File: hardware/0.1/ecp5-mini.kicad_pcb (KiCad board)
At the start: 4 copper layers, 52 x 27 mm, 64 parts, among them J1 Micro_SD_Card, J2 JTAG, J3 S7 Mini, J4 S7 Mini, J5 USB_C_Receptacle_USB2.0, Q1 BSS138, SW1 SW_Push, U1 ECP5U_12_CABGA256, U2 TLV73325PDBV, U3 TLV62568DBV, U4 USBLC6-2SC6, U5 TLV62568DBV, U6 W25Q128JVSIQ, U7 S27KL0641

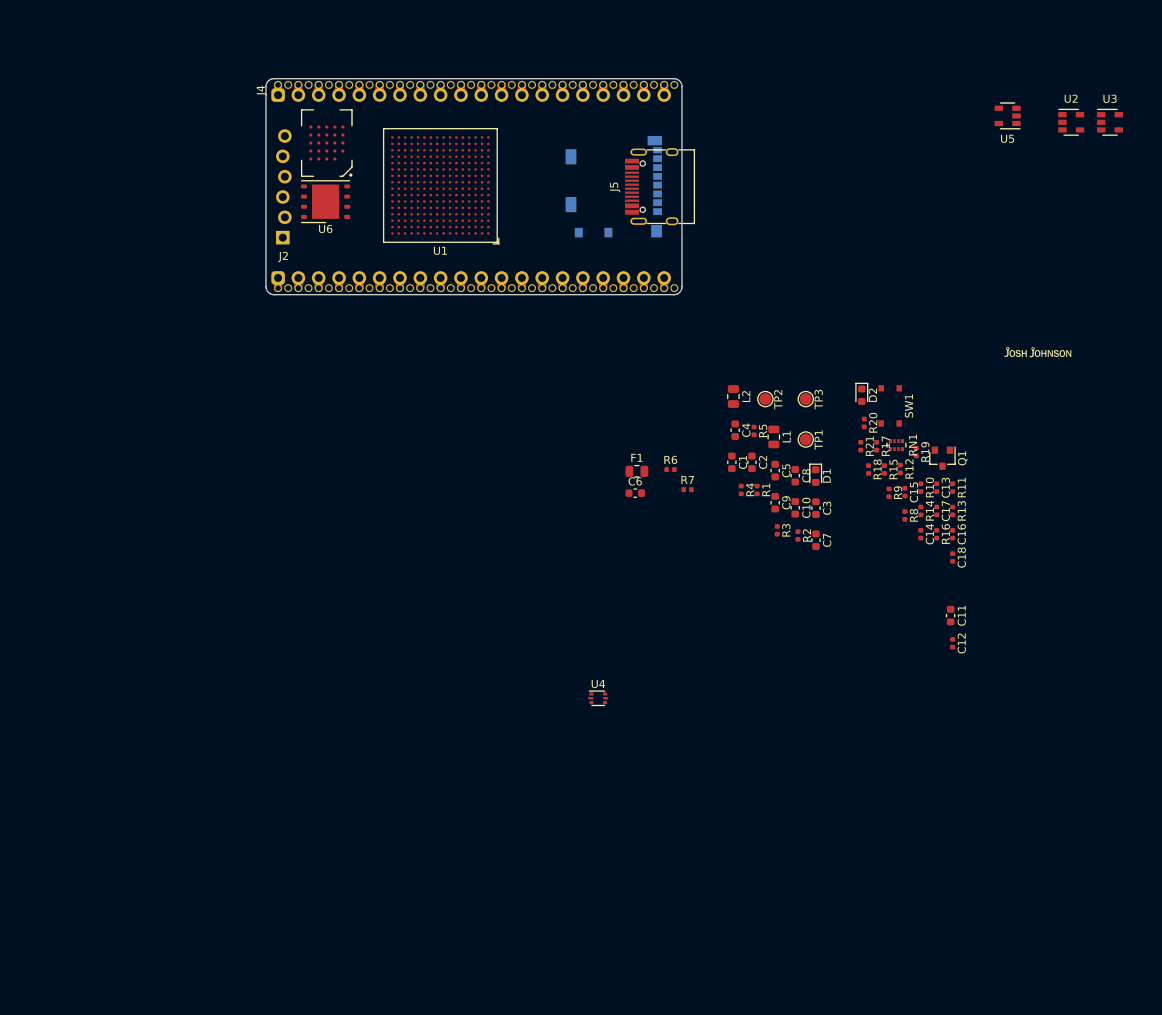
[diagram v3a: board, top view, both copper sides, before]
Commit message: all 3d models added
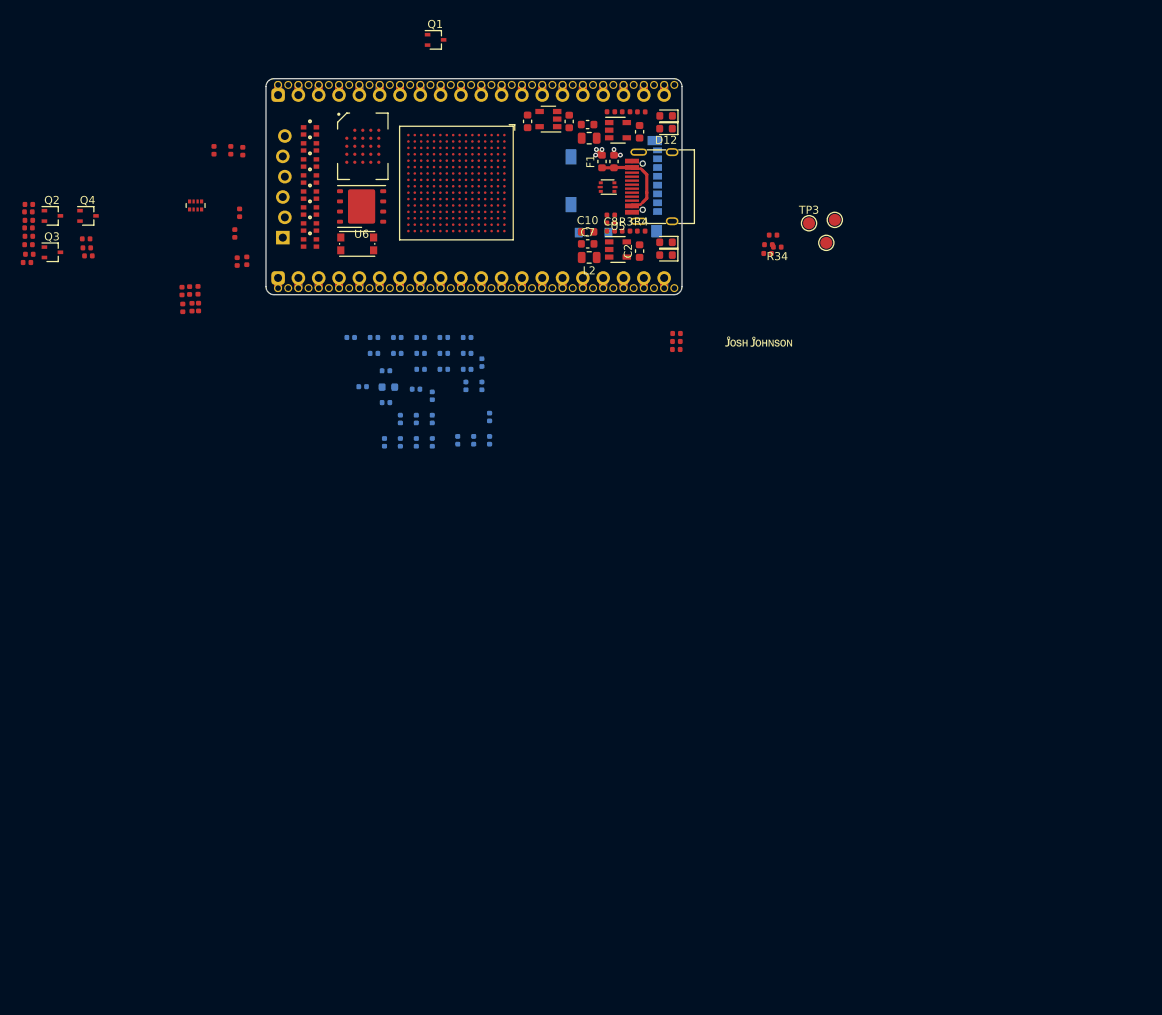
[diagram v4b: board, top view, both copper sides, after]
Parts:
- added C19: 100n, Capacitor_SMD:C_0402_1005Metric, B.Cu at (118.4, 117.8)
- added C20: 100n, Capacitor_SMD:C_0402_1005Metric, B.Cu at (121.3, 113.8)
- added C21: 100n, Capacitor_SMD:C_0402_1005Metric, B.Cu at (118.4, 115.8)
- added C22: 100n, Capacitor_SMD:C_0402_1005Metric, B.Cu at (120.2, 126.7)
- added C23: 470n, Capacitor_SMD:C_0402_1005Metric, B.Cu at (115.5, 115.8)
- added C24: 470n, Capacitor_SMD:C_0402_1005Metric, B.Cu at (124.2, 126.7)
- added C25: 100n, Capacitor_SMD:C_0402_1005Metric, B.Cu at (112.6, 113.8)
- added C26: 100n, Capacitor_SMD:C_0402_1005Metric, B.Cu at (115.5, 117.8)
- added C27: 100n, Capacitor_SMD:C_0402_1005Metric, B.Cu at (121.3, 115.8)
- added C28: 100n, Capacitor_SMD:C_0402_1005Metric, B.Cu at (112.6, 115.8)
- added C29: 470n, Capacitor_SMD:C_0402_1005Metric, B.Cu at (118.4, 113.8)
- added C30: 470n, Capacitor_SMD:C_0402_1005Metric, B.Cu at (121.3, 117.8)
- added C31: 100n, Capacitor_SMD:C_0402_1005Metric, B.Cu at (124.2, 123.7)
- added C32: 100n, Capacitor_SMD:C_0402_1005Metric, B.Cu at (109.7, 113.8)
- added C33: 100n, Capacitor_SMD:C_0402_1005Metric, B.Cu at (106.8, 113.8)
- added C34: 100n, Capacitor_SMD:C_0402_1005Metric, B.Cu at (109.7, 115.8)
- added C35: 470n, Capacitor_SMD:C_0402_1005Metric, B.Cu at (122.2, 126.7)
- added C36: 470n, Capacitor_SMD:C_0402_1005Metric, B.Cu at (115.5, 113.8)
- added C37: 100n, Capacitor_SMD:C_0402_1005Metric, B.Cu at (117.0, 124.0)
- added C38: 100n, Capacitor_SMD:C_0402_1005Metric, B.Cu at (115.0, 124.0)
- added C39: 100n, Capacitor_SMD:C_0402_1005Metric, B.Cu at (115.0, 126.9)
- added C40: 100n, Capacitor_SMD:C_0402_1005Metric, B.Cu at (117.0, 126.9)
- added C41: 100n, Capacitor_SMD:C_0402_1005Metric, B.Cu at (113.0, 124.0)
- added C42: 100n, Capacitor_SMD:C_0402_1005Metric, B.Cu at (111.0, 126.9)
- added C43: 100n, Capacitor_SMD:C_0402_1005Metric, B.Cu at (117.0, 121.1)
- added C44: 100n, Capacitor_SMD:C_0402_1005Metric, B.Cu at (113.0, 126.9)
- added C45: 100n, Capacitor_SMD:C_0402_1005Metric, B.Cu at (123.2, 116.9)
- added C46: 100n, Capacitor_SMD:C_0402_1005Metric, B.Cu at (123.2, 119.8)
- added C47: 100n, Capacitor_SMD:C_0402_1005Metric, B.Cu at (121.2, 119.8)
- added D10: LED_RGBA, josh-led:LED_0606_E6C0606RGBC3UDA, F.Cu at (101.7, 102.0)
- added D11: LED_RGBA, josh-led:LED_0606_E6C0606RGBC3UDA, F.Cu at (101.7, 88.0)
- added D12: PINK, LED_SMD:LED_0603_1608Metric, F.Cu at (146.2, 87.7)
- added D3: PINK, LED_SMD:LED_0603_1608Metric, F.Cu at (146.2, 86.1)
- added D4: LED_RGBA, josh-led:LED_0606_E6C0606RGBC3UDA, F.Cu at (101.7, 92.0)
- added D5: LED_RGBA, josh-led:LED_0606_E6C0606RGBC3UDA, F.Cu at (101.7, 90.0)
- added D6: LED_RGBA, josh-led:LED_0606_E6C0606RGBC3UDA, F.Cu at (101.7, 94.0)
- added D7: LED_RGBA, josh-led:LED_0606_E6C0606RGBC3UDA, F.Cu at (101.7, 100.0)
- added D8: LED_RGBA, josh-led:LED_0606_E6C0606RGBC3UDA, F.Cu at (101.7, 98.0)
- added D9: LED_RGBA, josh-led:LED_0606_E6C0606RGBC3UDA, F.Cu at (101.7, 96.0)
- added Q2: BSS138, Package_TO_SOT_SMD:SOT-323_SC-70, F.Cu at (69.5, 98.6)
- added Q3: BSS138, Package_TO_SOT_SMD:SOT-323_SC-70, F.Cu at (69.5, 103.2)
- added Q4: BSS138, Package_TO_SOT_SMD:SOT-323_SC-70, F.Cu at (74.0, 98.6)
- added R22: 1K5, Resistor_SMD:R_0402_1005Metric, F.Cu at (158.9, 103.3)
- added R23: 220R, Resistor_SMD:R_0402_1005Metric, F.Cu at (66.6, 101.2)
- added R24: 220R, Resistor_SMD:R_0402_1005Metric, F.Cu at (66.6, 97.2)
- added R25: 10K, Resistor_SMD:R_0402_1005Metric, F.Cu at (73.8, 102.6)
- added R26: 220R, Resistor_SMD:R_0402_1005Metric, F.Cu at (66.5, 102.2)
- added R27: 220R, Resistor_SMD:R_0402_1005Metric, F.Cu at (66.3, 104.4)
- added R28: 10K, Resistor_SMD:R_0402_1005Metric, F.Cu at (73.7, 101.5)
- added R29: 220R, Resistor_SMD:R_0402_1005Metric, F.Cu at (66.6, 99.2)
- added R30: 10K, Resistor_SMD:R_0402_1005Metric, F.Cu at (74.0, 103.6)
- added R31: 220R, Resistor_SMD:R_0402_1005Metric, F.Cu at (66.5, 100.1)
- added R32: 220R, Resistor_SMD:R_0402_1005Metric, F.Cu at (66.5, 98.1)
- added R33: 220R, Resistor_SMD:R_0402_1005Metric, F.Cu at (66.6, 103.4)
- added R34: 1K5, Resistor_SMD:R_0402_1005Metric, F.Cu at (160.1, 102.5)
- C10: value 6p8 -> 22u
- C11, C12, C14, C16, C17: moved to B.Cu
- C8: value 22u -> 6p8; footprint Capacitor_SMD:C_0603_1608Metric -> Capacitor_SMD:C_0402_1005Metric
- C9: footprint Capacitor_SMD:C_0603_1608Metric -> Capacitor_SMD:C_0402_1005Metric
- F1: footprint josh-passives-smt:Fuse_0805_2012Metric -> josh-passives-smt:Fuse_0603_1608Metric
- J1: footprint Connector_Card:microSD_HC_Molex_104031-0811 -> josh-mechanical:microSD_HC_Molex_104031-0811
- Q1: footprint Package_TO_SOT_SMD:SOT-23 -> Package_TO_SOT_SMD:SOT-323_SC-70
- R5: value 5K1 -> 1K5
- SW1: footprint josh-buttons-switches:SW_Push_PTS815 -> josh-buttons-switches:SW_Push_KMR2
- U6: footprint Package_SON:WSON-8-1EP_6x5mm_P1.27mm_EP3.4x4.3mm -> josh-soic-sot-etc:WSON-8-1EP_6x5mm_P1.27mm_EP3.4x4.3mm
- moved C18 98.5 mm to (92.3, 100.8)
- moved R13 97.6 mm to (87.8, 110.0)
- moved R16 97.3 mm to (87.0, 110.0)
- moved R14 95.7 mm to (85.8, 110.1)
- moved R19 93.6 mm to (91.8, 90.4)
- moved C15 93.1 mm to (93.3, 90.5)
- moved RN1 92.6 mm to (87.4, 97.3)
- moved C13 91.9 mm to (92.6, 104.3)
- moved R8 91.4 mm to (92.9, 98.2)
- moved R17 89.0 mm to (85.7, 108.0)
- moved R15 88.7 mm to (87.7, 107.9)
- moved R20 88.1 mm to (89.7, 90.4)
- moved R18 87.8 mm to (86.7, 107.9)
- moved R12 85.7 mm to (93.8, 104.2)
- moved Q1 82.1 mm to (117.4, 76.6), turned to 0 degrees
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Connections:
- net Net-(J3-Pad1) renamed /Board IO/PORT_A0
- net Net-(J3-Pad11) renamed /Board IO/PORT_B0
- net Net-(J3-Pad12) renamed /Board IO/PORT_B4
- net Net-(J3-Pad13) renamed /Board IO/PORT_B1
- net Net-(J3-Pad14) renamed /Board IO/PORT_B5
- net Net-(J3-Pad15) renamed /Board IO/PORT_B2
- net Net-(J3-Pad16) renamed /Board IO/PORT_B6
- net Net-(J3-Pad17) renamed /Board IO/PORT_B3
- net Net-(J3-Pad18) renamed /Board IO/PORT_B7
- net Net-(J3-Pad2) renamed /Board IO/PORT_A4
- net Net-(J3-Pad21) renamed /Board IO/PORT_C0
- net Net-(J3-Pad22) renamed /Board IO/PORT_C4
- net Net-(J3-Pad23) renamed /Board IO/PORT_C1
- net Net-(J3-Pad24) renamed /Board IO/PORT_C5
- net Net-(J3-Pad25) renamed /Board IO/PORT_C2
- net Net-(J3-Pad26) renamed /Board IO/PORT_C6
- net Net-(J3-Pad27) renamed /Board IO/PORT_C3
- net Net-(J3-Pad28) renamed /Board IO/PORT_C7
- net Net-(J3-Pad3) renamed /Board IO/PORT_A1
- net Net-(J3-Pad31) renamed /Board IO/PORT_D0
- net Net-(J3-Pad32) renamed /Board IO/PORT_D4
- net Net-(J3-Pad33) renamed /Board IO/PORT_D1
- net Net-(J3-Pad34) renamed /Board IO/PORT_D5
- net Net-(J3-Pad35) renamed /Board IO/PORT_D2
- net Net-(J3-Pad36) renamed /Board IO/PORT_D6
- net Net-(J3-Pad37) renamed /Board IO/PORT_D3
- net Net-(J3-Pad38) renamed /Board IO/PORT_D7
- net Net-(J3-Pad4) renamed /Board IO/PORT_A5
- net Net-(J3-Pad5) renamed /Board IO/PORT_A2
- net Net-(J3-Pad6) renamed /Board IO/PORT_A6
- net Net-(J3-Pad7) renamed /Board IO/PORT_A3
- net Net-(J3-Pad8) renamed /Board IO/PORT_A7
- net Net-(J4-Pad21) renamed /Board IO/PORT_F0
- net Net-(J4-Pad22) renamed /Board IO/PORT_F4
- net Net-(J4-Pad23) renamed /Board IO/PORT_F1
- net Net-(J4-Pad24) renamed /Board IO/PORT_F5
- net Net-(J4-Pad25) renamed /Board IO/PORT_F2
- net Net-(J4-Pad26) renamed /Board IO/PORT_F6
- net Net-(J4-Pad27) renamed /Board IO/PORT_F3
- net Net-(J4-Pad28) renamed /Board IO/PORT_F7
- net Net-(J4-Pad31) renamed /Board IO/PORT_E0
- net Net-(J4-Pad32) renamed /Board IO/PORT_E4
- net Net-(J4-Pad33) renamed /Board IO/PORT_E1
- net Net-(J4-Pad34) renamed /Board IO/PORT_E5
- net Net-(J4-Pad35) renamed /Board IO/PORT_E2
- net Net-(J4-Pad36) renamed /Board IO/PORT_E6
- net Net-(J4-Pad37) renamed /Board IO/PORT_E3
- net Net-(J4-Pad38) renamed /Board IO/PORT_E7
- net Net-(U7-PadA3) renamed /Hyperram / Micro SD/nCS
- net Net-(U7-PadA4) renamed /Hyperram / Micro SD/nRST
- net Net-(U7-PadB1) renamed /Hyperram / Micro SD/nCK
- net Net-(U7-PadB2) renamed /Hyperram / Micro SD/CK
- net Net-(U7-PadC3) renamed /Hyperram / Micro SD/RWDS
- net Net-(U7-PadC4) renamed /Hyperram / Micro SD/DQ2
- net Net-(U7-PadD2) renamed /Hyperram / Micro SD/DQ1
- net Net-(U7-PadD3) renamed /Hyperram / Micro SD/DQ0
- net Net-(U7-PadD4) renamed /Hyperram / Micro SD/DQ3
- net Net-(U7-PadD5) renamed /Hyperram / Micro SD/DQ4
- net Net-(U7-PadE1) renamed /Hyperram / Micro SD/DQ7
- net Net-(U7-PadE2) renamed /Hyperram / Micro SD/DQ6
- net Net-(U7-PadE3) renamed /Hyperram / Micro SD/DQ5
- C10 pad 2: Net-(C10-Pad2) -> GND
- C5 pad 2: Net-(C5-Pad2) -> GND
- C7 pad 2: Net-(C10-Pad2) -> GND
- C8 pad 2: Net-(C10-Pad2) -> Net-(C8-Pad2)
- C9 pad 2: Net-(C5-Pad2) -> Net-(C9-Pad2)
- J3 pad 10: Net-(J3-Pad10) -> GND
- J3 pad 19: Net-(J3-Pad19) -> +3V3
- J3 pad 20: Net-(J3-Pad20) -> GND
- J3 pad 29: Net-(J3-Pad29) -> GND
- J3 pad 30: Net-(J3-Pad30) -> GND
- J3 pad 39: Net-(J3-Pad39) -> +5V
- J3 pad 40: Net-(J3-Pad40) -> GND
- J3 pad 9: Net-(J3-Pad9) -> GND
- J4 pad 1: Net-(J4-Pad1) -> /Board IO/PORT_G0
- J4 pad 10: Net-(J4-Pad10) -> GND
- J4 pad 11: Net-(J4-Pad11) -> /Board IO/PORT_G0
- J4 pad 12: Net-(J4-Pad12) -> /Board IO/PORT_G4
- J4 pad 13: Net-(J4-Pad13) -> /Board IO/PORT_G1
- J4 pad 14: Net-(J4-Pad14) -> /Board IO/PORT_G5
- J4 pad 15: Net-(J4-Pad15) -> /Board IO/PORT_G2
- J4 pad 16: Net-(J4-Pad16) -> /Board IO/PORT_G6
- J4 pad 17: Net-(J4-Pad17) -> /Board IO/PORT_G3
- J4 pad 18: Net-(J4-Pad18) -> /Board IO/PORT_G7
- J4 pad 19: Net-(J4-Pad19) -> +3V3
- J4 pad 2: Net-(J4-Pad2) -> /Board IO/PORT_G4
- J4 pad 20: Net-(J4-Pad20) -> GND
- J4 pad 29: Net-(J4-Pad29) -> GND
- J4 pad 3: Net-(J4-Pad3) -> /Board IO/PORT_G1
- J4 pad 30: Net-(J4-Pad30) -> GND
- J4 pad 39: Net-(J4-Pad39) -> +5V
- J4 pad 4: Net-(J4-Pad4) -> /Board IO/PORT_G5
- J4 pad 40: Net-(J4-Pad40) -> GND
- J4 pad 5: Net-(J4-Pad5) -> /Board IO/PORT_G2
- J4 pad 6: Net-(J4-Pad6) -> /Board IO/PORT_G6
- J4 pad 7: Net-(J4-Pad7) -> /Board IO/PORT_G3
- J4 pad 8: Net-(J4-Pad8) -> /Board IO/PORT_G7
- J4 pad 9: Net-(J4-Pad9) -> GND
- R1 pad 2: Net-(C5-Pad2) -> Net-(C9-Pad2)
- R2 pad 1: Net-(C5-Pad2) -> Net-(C9-Pad2)
- R3 pad 2: Net-(C10-Pad2) -> Net-(C8-Pad2)
- R4 pad 1: Net-(C10-Pad2) -> Net-(C8-Pad2)
- R5 pad 1: +5V -> +3V3
- U1 pad A1: Net-(U1-PadA1) -> GND
- U1 pad A16: Net-(U1-PadA1) -> GND
- U1 pad D15: Net-(U1-PadA1) -> GND
- U1 pad D2: Net-(U1-PadA1) -> GND
- U1 pad F10: Net-(U1-PadF10) -> +3V3
- U1 pad F11: Net-(U1-PadF10) -> +3V3
- U1 pad F6: Net-(U1-PadF6) -> +3V3
- U1 pad F7: Net-(U1-PadF6) -> +3V3
- U1 pad F8: Net-(U1-PadA1) -> GND
- U1 pad F9: Net-(U1-PadA1) -> GND
- U1 pad G10: Net-(U1-PadA1) -> GND
- U1 pad G11: Net-(U1-PadG11) -> +2V5
- U1 pad G6: Net-(U1-PadG6) -> +1V1
- U1 pad G7: Net-(U1-PadG6) -> +1V1
- U1 pad G8: Net-(U1-PadA1) -> GND
- U1 pad G9: Net-(U1-PadG6) -> +1V1
- U1 pad H1: Net-(U1-PadA1) -> GND
- U1 pad H10: Net-(U1-PadA1) -> GND
- U1 pad H11: Net-(U1-PadH11) -> +3V3
- U1 pad H16: Net-(U1-PadA1) -> GND
- U1 pad H6: Net-(U1-PadH6) -> +3V3
- U1 pad H7: Net-(U1-PadH6) -> +3V3
- U1 pad H8: Net-(U1-PadA1) -> GND
- U1 pad H9: Net-(U1-PadA1) -> GND
- U1 pad J10: Net-(U1-PadA1) -> GND
- U1 pad J11: Net-(U1-PadH11) -> +3V3
- U1 pad J6: Net-(U1-PadJ6) -> +3V3
- U1 pad J7: Net-(U1-PadJ6) -> +3V3
- U1 pad J8: Net-(U1-PadA1) -> GND
- U1 pad J9: Net-(U1-PadA1) -> GND
- U1 pad K10: Net-(U1-PadA1) -> GND
- U1 pad K11: Net-(U1-PadK11) -> +3V3
- U1 pad K6: Net-(U1-PadA1) -> GND
- U1 pad K7: Net-(U1-PadA1) -> GND
- U1 pad K8: Net-(U1-PadA1) -> GND
- U1 pad K9: Net-(U1-PadA1) -> GND
- U1 pad L10: Net-(U1-PadG6) -> +1V1
- U1 pad L11: Net-(U1-PadK11) -> +3V3
- U1 pad L7: Net-(U1-PadG11) -> +2V5
- U1 pad L8: Net-(U1-PadG6) -> +1V1
- U1 pad L9: Net-(U1-PadG6) -> +1V1
- U1 pad N15: Net-(U1-PadA1) -> GND
- U1 pad N2: Net-(U1-PadA1) -> GND
- U1 pad R6: Net-(U1-PadR6) -> /FPGA Config/FPGA_OK
- U1 pad T1: Net-(U1-PadA1) -> GND
- U1 pad T12: Net-(U1-PadA1) -> GND
- U1 pad T16: Net-(U1-PadA1) -> GND
- U1 pad T5: Net-(U1-PadA1) -> GND
- U1 pad T6: Net-(U1-PadT6) -> /FPGA Config/LED_USR
- U3 pad 5: Net-(C5-Pad2) -> Net-(C9-Pad2)
- U5 pad 5: Net-(C10-Pad2) -> Net-(C8-Pad2)
- U7 pad B3: Net-(U7-PadB3) -> GND
- U7 pad B4: Net-(U7-PadB4) -> +3V3
- U7 pad C1: Net-(U7-PadC1) -> GND
- U7 pad D1: Net-(U7-PadD1) -> +3V3
- U7 pad E4: Net-(U7-PadE4) -> +3V3
- U7 pad E5: Net-(U7-PadE5) -> GND
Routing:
- net +5V: track 0.00 -> 42.2 mm, vias 0 -> 3
- net Net-(C6-Pad1): track 0.00 -> 13.5 mm
- net GND: track 0.00 -> 1.82 mm, vias 0 -> 2
- added copper zone on In2.Cu, net +3V3
- added copper zone on In1.Cu, net GND

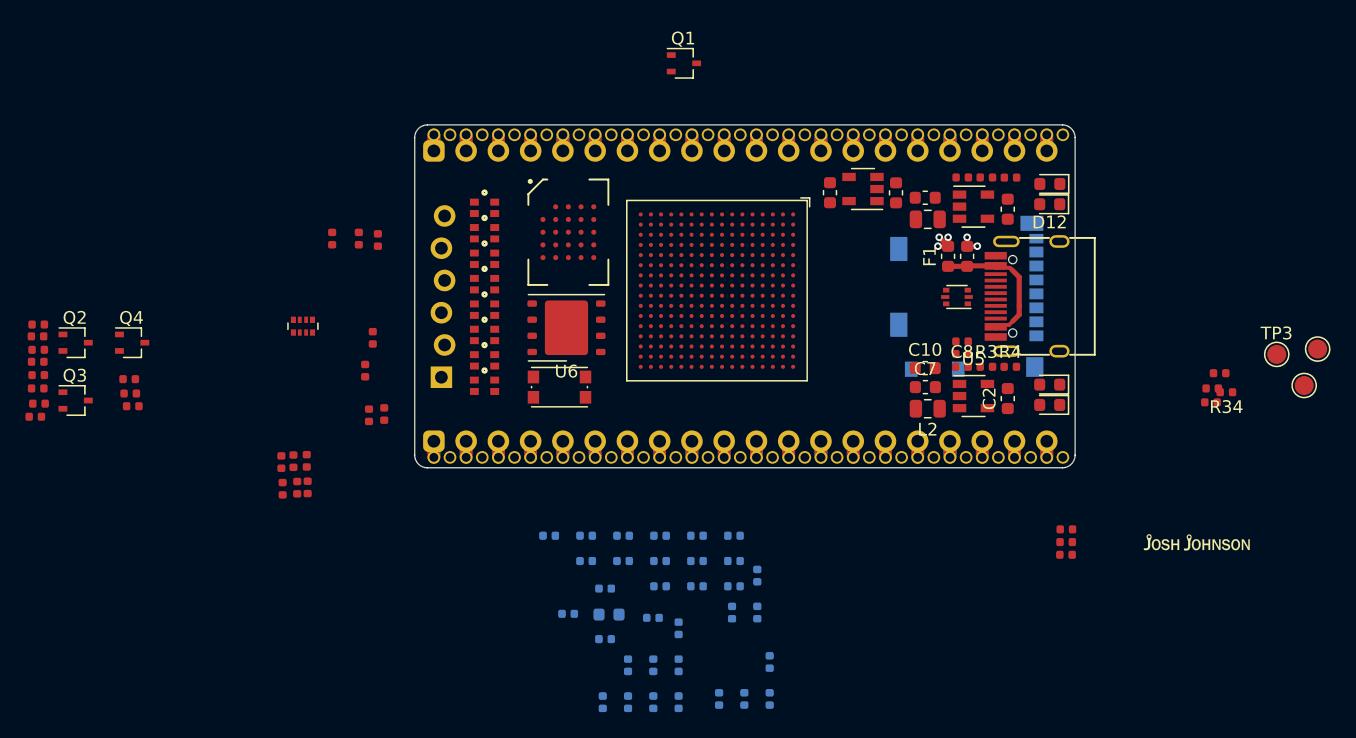
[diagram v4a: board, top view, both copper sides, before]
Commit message: decoupling down + outer pins fanned out
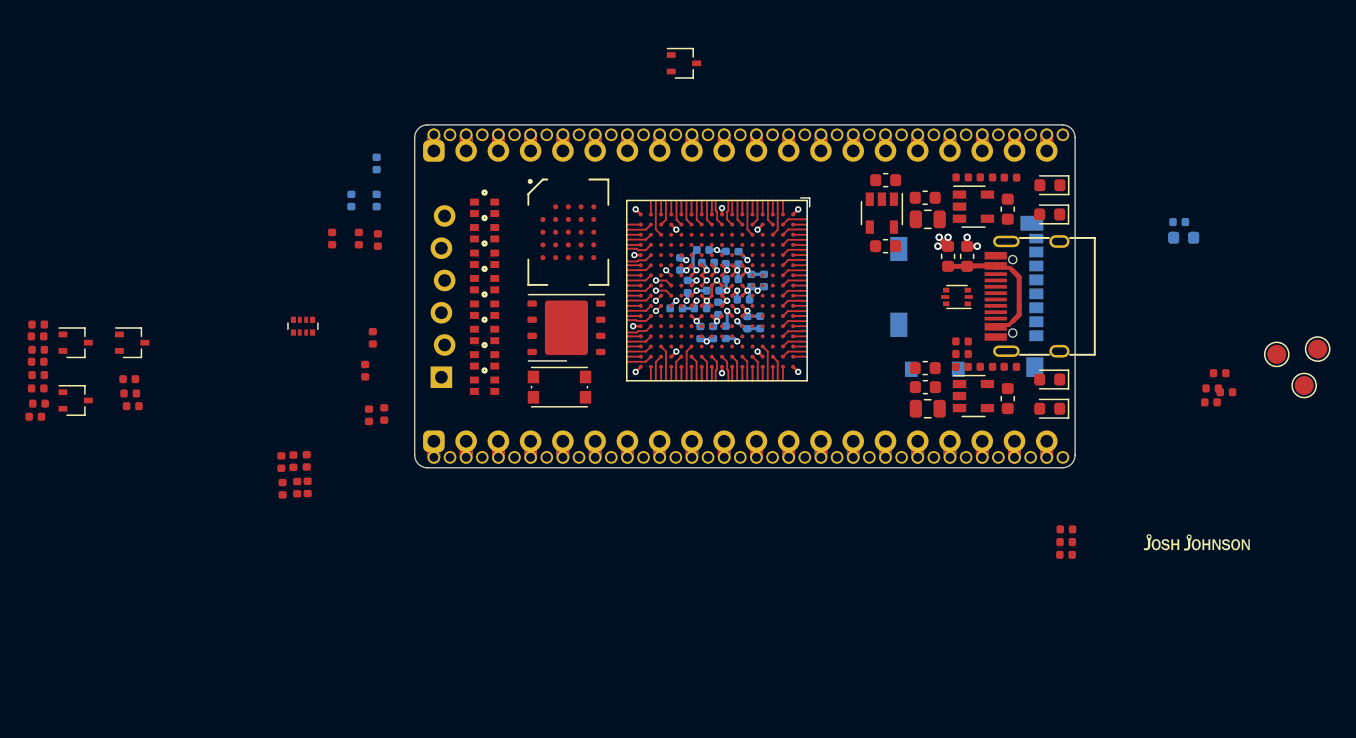
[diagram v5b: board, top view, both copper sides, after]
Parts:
- removed C14, C24, C35, C36: 470n, Capacitor_SMD:C_0402_1005Metric
- removed C16, C27, C28, C33, C34, C44: 100n, Capacitor_SMD:C_0402_1005Metric
- C21, C22: value 100n -> 4u7
- C23, C29, C30: value 470n -> 4u7
- moved C11 54.1 mm to (156.8, 90.3)
- moved C12 51.9 mm to (156.4, 89.1)
- moved C45 44.2 mm to (93.2, 84.5)
- moved C46 44.2 mm to (93.2, 87.4)
- moved C47 44.2 mm to (91.2, 87.4)
- moved C40 35.7 mm to (118.9, 91.3), turned to 0 degrees
- moved C22 34.8 mm to (121.7, 91.9)
- moved C42 33.6 mm to (122.1, 95.2), turned to 0 degrees
- moved C39 32.7 mm to (119.7, 94.5), turned to 0 degrees
- moved C31 32.0 mm to (120.7, 91.9)
- moved C41 31.5 mm to (121.2, 93.6), turned to 180 degrees
- moved C17 28.9 mm to (117.1, 92.4), turned to 90 degrees
- moved C37 28.2 mm to (118.7, 95.9), turned to 0 degrees
- moved C43 26.9 mm to (117.7, 94.2), turned to -90 degrees
- moved C38 26.8 mm to (120.7, 97.8), turned to -90 degrees
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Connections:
- C21 pad 1: +3V3 -> +1V1
- C22 pad 1: +3V3 -> +1V1
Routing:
- net GND: track 1.82 -> 33.7 mm, vias 2 -> 31
- net +3V3: track 0.00 -> 13.2 mm, vias 0 -> 7
- net +1V1: track 0.00 -> 11.7 mm, vias 0 -> 5
- net +2V5: track 0.00 -> 4.21 mm, vias 0 -> 2
- net Net-(U1-PadD14): track 0.00 -> 2.87 mm
- net Net-(U1-PadE3): track 0.00 -> 2.87 mm
- net Net-(U1-PadP3): track 0.00 -> 2.86 mm
- net Net-(U1-PadP14): track 0.00 -> 2.84 mm
- net Net-(U1-PadL14): track 0.00 -> 2.84 mm
- net Net-(U1-PadC3): track 0.00 -> 2.84 mm
- net Net-(U1-PadR4): track 0.00 -> 2.12 mm
- net Net-(U1-PadG2): track 0.00 -> 2.11 mm
- net Net-(U1-PadH15): track 0.00 -> 2.11 mm
- net Net-(U1-PadR5): track 0.00 -> 2.11 mm
- net Net-(U1-PadR12): track 0.00 -> 2.11 mm
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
